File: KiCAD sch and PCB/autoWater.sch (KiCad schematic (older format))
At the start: 14 parts

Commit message: some sch changes
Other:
- note added: "делитель для датчика почвы продумать"
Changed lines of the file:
@@
 Wire Wire Line
 	5050 1450 5050 1400
+Text Notes 7700 3850 0    50   ~ 0
+делитель для датчика почвы продумать
 $EndSCHEMATC

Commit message: some commit
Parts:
- removed Q?: 2N3904, Package_TO_SOT_THT:TO-92_Inline, symbol Transistor_BJT:2N3904
- removed R?: 220, symbol Device:R
- added J2: PROG, Connector_PinHeader_2.54mm:PinHeader_1x05_P2.54mm_Vertical, symbol Connector:Conn_01x05_Male
- added Q2: AO3400, Package_TO_SOT_SMD:SOT-23, symbol Device:Q_NMOS_GSD
- added R3: 1.5k, Resistor_THT:R_Axial_DIN0411_L9.9mm_D3.6mm_P15.24mm_Horizontal, symbol Device:R
- added R5: 10k, Resistor_SMD:R_0805_2012Metric_Pad1.15x1.40mm_HandSolder, symbol Device:R
- added SW1: SW_Push_Dual, Button_Switch_SMD:SW_SPST_Omron_B3FS-100xP, symbol Switch:SW_Push_Dual
- C1: renamed from C?; footprint (none) -> Capacitor_SMD:C_0805_2012Metric_Pad1.15x1.40mm_HandSolder
- D1: renamed from D?; footprint (none) -> LED_SMD:LED_0805_2012Metric_Pad1.15x1.40mm_HandSolder
- J1, J3, J4: renamed from J?; footprint (none) -> Connector_PinHeader_2.54mm:PinHeader_1x02_P2.54mm_Vertical
- Q1: renamed from Q?; footprint (none) -> Package_TO_SOT_SMD:SOT-23
- R1, R4, R6: renamed from R?; footprint (none) -> Resistor_SMD:R_0805_2012Metric_Pad1.15x1.40mm_HandSolder
- R2: renamed from R?; value 100k -> 4.7k; footprint (none) -> Resistor_THT:R_Axial_DIN0411_L9.9mm_D3.6mm_P15.24mm_Horizontal
- R7: renamed from R?; value 130k -> 150k; footprint (none) -> Resistor_SMD:R_0805_2012Metric_Pad1.15x1.40mm_HandSolder
- gave numbers to parts that had none: 1
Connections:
- net +5V: now also J2.4 (Pin_4)
- net GND: now also J2.5 (Pin_5), Q2.2 (S), R3.2, R5.2, SW1.2, SW1.4; no longer R2.2
- net Sensor: no longer U1.3 (PB4)
- net Button: now reaches U1.1 (~RESET~/PB5)
- net Button: now also SW1.1, SW1.3
- net at U1.2 (PB3): now also Q2.1 (G), R5.1
- net at R1.2, U1.5 (PB0): now also J2.2 (Pin_2)
- net at Q1.1 (G), R4.1, U1.6 (PB1): now also J2.3 (Pin_3)
- net at R6.2, R7.1, U1.7 (PB2): now also J2.1 (Pin_1)
- net at J3.2 (Pin_2): now also Q2.3 (D)
- new net: R2.2, R3.1, U1.3 (PB4)
- no-connect marks 1 -> 0
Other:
- note added: "2n3904 + 220 Ohm"
- note added: "делитель нужен, чтобы понизить\nнапряжения для сравнения с\nопорным 1.1В"
- note removed: "делитель для датчика почвы продумать"
- moved on the sheet: J3, R2

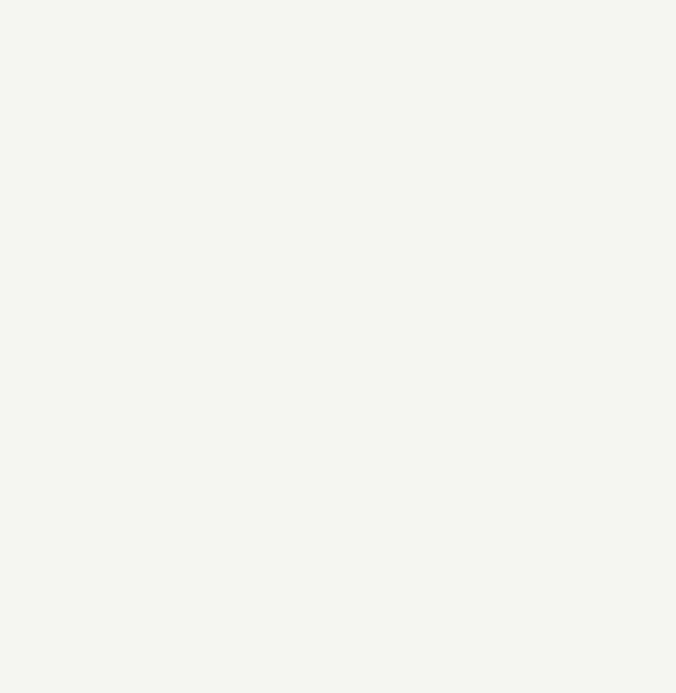
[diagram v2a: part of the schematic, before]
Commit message: added li ion charger on pcb
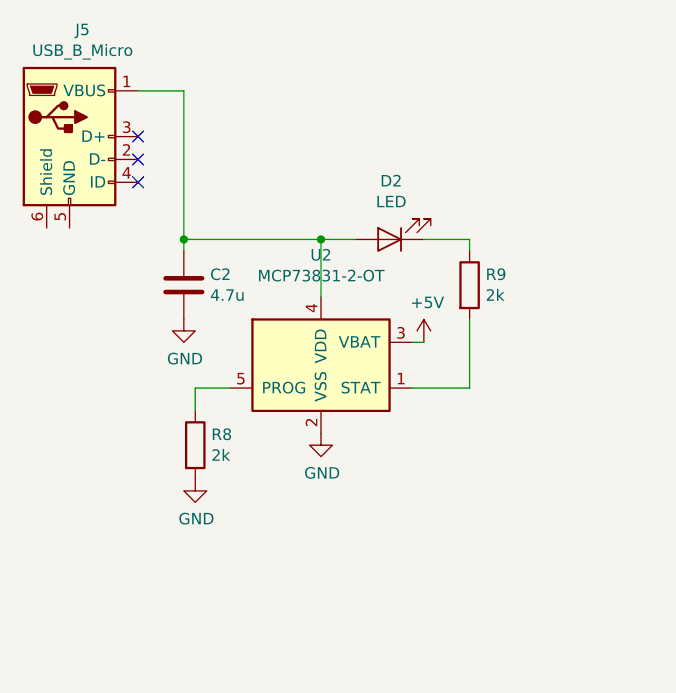
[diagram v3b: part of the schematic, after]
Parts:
- added C2: 4.7u, Capacitor_SMD:C_0805_2012Metric_Pad1.15x1.40mm_HandSolder, symbol Device:C
- added D2: LED, LED_SMD:LED_0805_2012Metric_Pad1.15x1.40mm_HandSolder, symbol Device:LED
- added J5: USB_B_Micro, Connector_USB:USB_Micro-B_Wuerth_629105150521, symbol Connector:USB_B_Micro
- added R8, R9: 2k, Resistor_SMD:R_0805_2012Metric_Pad1.15x1.40mm_HandSolder, symbol Device:R
- added U2: MCP73831-2-OT, Package_TO_SOT_SMD:SOT-23-5, symbol Battery_Management:MCP73831-2-OT
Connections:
- net +5V: now also U2.3 (VBAT)
- net GND: now also C2.2, R8.2, U2.2 (VSS)
- new net: C2.1, D2.2 (A), J5.1 (VBUS), U2.4 (VDD)
- new net: R8.1, U2.5 (PROG)
- new net: D2.1 (K), R9.1
- new net: R9.2, U2.1 (STAT)
- no-connect marks 0 -> 3
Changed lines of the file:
@@
 	8800 5000 8800 5200
 Connection ~ 8800 5200
+$Comp
+L Connector:USB_B_Micro J5
+U 1 1 5ED77C14
+P 1000 1150
+F 0 "J5" H 1057 1617 50  0000 C CNN
+F 1 "USB_B_Micro" H 1057 1526 50  0000 C CNN
+F 2 "Connector_USB:USB_Micro-B_Wuerth_629105150521" H 1150 1100 50  0001 C CNN
+F 3 "~" H 1150 1100 50  0001 C CNN
+	1    1000 1150
+	1    0    0    -1
+$EndComp
+NoConn ~ 1300 1150
+NoConn ~ 1300 1250
+NoConn ~ 1300 1350
+$Comp
+L Device:R R8
+U 1 1 5ED7E586
+P 1550 2500
+F 0 "R8" H 1620 2546 50  0000 L CNN
+F 1 "2k" H 1620 2455 50  0000 L CNN
+F 2 "Resistor_SMD:R_0805_2012Metric_Pad1.15x1.40mm_HandSolder" V 1480 2500 50  0001 C CNN
+F 3 "~" H 1550 2500 50  0001 C CNN
+	1    1550 2500
+	1    0    0    -1
+$EndComp
+$Comp
+L Battery_Management:MCP73831-2-OT U2
+U 1 1 5ED87504
+P 2100 2150
+F 0 "U2" H 2100 2631 50  0000 C CNN
+F 1 "MCP73831-2-OT" H 2100 2540 50  0000 C CNN
+F 2 "Package_TO_SOT_SMD:SOT-23-5" H 2150 1900 50  0001 L CIN
+F 3 "http://ww1.microchip.com/downloads/en/DeviceDoc/20001984g.pdf" H 1950 2100 50  0001 C CNN
+	1    2100 2150
+	1    0    0    -1
+$EndComp
+Wire Wire Line
+	1700 2250 1550 2250
+Wire Wire Line
+	1550 2250 1550 2350
+$Comp
+L power:GND #PWR02
+U 1 1 5ED80F71
+P 1550 2650
+F 0 "#PWR02" H 1550 2400 50  0001 C CNN
+F 1 "GND" H 1555 2477 50  0000 C CNN
+F 2 "" H 1550 2650 50  0001 C CNN
+F 3 "" H 1550 2650 50  0001 C CNN
+	1    1550 2650
+	1    0    0    -1
+$EndComp
+$Comp
+L power:GND #PWR03
+U 1 1 5ED8174D
+P 2100 2450
+F 0 "#PWR03" H 2100 2200 50  0001 C CNN
+F 1 "GND" H 2105 2277 50  0000 C CNN
+F 2 "" H 2100 2450 50  0001 C CNN
+F 3 "" H 2100 2450 50  0001 C CNN
+	1    2100 2450
+	1    0    0    -1
+$EndComp
+$Comp
+L Device:LED D2
+U 1 1 5ED81BE4
+P 2400 1600
+F 0 "D2" H 2393 1345 50  0000 C CNN
+F 1 "LED" H 2393 1436 50  0000 C CNN
+F 2 "LED_SMD:LED_0805_2012Metric_Pad1.15x1.40mm_HandSolder" H 2400 1600 50  0001 C CNN
+F 3 "~" H 2400 1600 50  0001 C CNN
+	1    2400 1600
+	-1   0    0    1
+$EndComp
+$Comp
+L Device:R R9
+U 1 1 5ED82954
+P 2750 1800
+F 0 "R9" H 2820 1846 50  0000 L CNN
+F 1 "2k" H 2820 1755 50  0000 L CNN
+F 2 "Resistor_SMD:R_0805_2012Metric_Pad1.15x1.40mm_HandSolder" V 2680 1800 50  0001 C CNN
+F 3 "~" H 2750 1800 50  0001 C CNN
+	1    2750 1800
+	1    0    0    -1
+$EndComp
+Wire Wire Line
+	2250 1600 2100 1600
+Wire Wire Line
+	2100 1600 2100 1850
+Wire Wire Line
+	2550 1600 2750 1600
+Wire Wire Line
+	2750 1600 2750 1650
+Wire Wire Line
+	2750 1950 2750 2250
+Wire Wire Line
+	2750 2250 2500 2250
+$Comp
+L Device:C C2
+U 1 1 5ED885A2
+P 1500 1800
+F 0 "C2" H 1615 1846 50  0000 L CNN
+F 1 "4.7u" H 1615 1755 50  0000 L CNN
+F 2 "Capacitor_SMD:C_0805_2012Metric_Pad1.15x1.40mm_HandSolder" H 1538 1650 50  0001 C CNN
+F 3 "~" H 1500 1800 50  0001 C CNN
+	1    1500 1800
+	1    0    0    -1
+$EndComp
+Wire Wire Line
+	2100 1600 1500 1600
+Wire Wire Line
+	1500 1600 1500 1650
+Connection ~ 2100 1600
+Wire Wire Line
+	1500 1600 1500 950
+Wire Wire Line
+	1500 950  1300 950
+Connection ~ 1500 1600
+$Comp
+L power:GND #PWR01
+U 1 1 5ED90F67
+P 1500 1950
+F 0 "#PWR01" H 1500 1700 50  0001 C CNN
+F 1 "GND" H 1505 1777 50  0000 C CNN
+F 2 "" H 1500 1950 50  0001 C CNN
+F 3 "" H 1500 1950 50  0001 C CNN
+	1    1500 1950
+	1    0    0    -1
+$EndComp
+$Comp
+L power:+5V #PWR04
+U 1 1 5ED912FB
+P 2550 2050
+F 0 "#PWR04" H 2550 1900 50  0001 C CNN
+F 1 "+5V" H 2565 2223 50  0000 C CNN
+F 2 "" H 2550 2050 50  0001 C CNN
+F 3 "" H 2550 2050 50  0001 C CNN
+	1    2550 2050
+	1    0    0    -1
+$EndComp
+Wire Wire Line
+	2500 2050 2550 2050
 $EndSCHEMATC

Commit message: same
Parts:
- R9: value 2k -> 470
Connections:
- net GND: now also J5.5 (GND), J5.6 (Shield)
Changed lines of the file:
@@
 P 2750 1800
 F 0 "R9" H 2820 1846 50  0000 L CNN
-F 1 "2k" H 2820 1755 50  0000 L CNN
+F 1 "470" H 2820 1755 50  0000 L CNN
 F 2 "Resistor_SMD:R_0805_2012Metric_Pad1.15x1.40mm_HandSolder" V 2680 1800 50  0001 C CNN
 F 3 "~" H 2750 1800 50  0001 C CNN
@@
 Wire Wire Line
 	2500 2050 2550 2050
+$Comp
+L power:GND #PWR0118
+U 1 1 5EDA0745
+P 1000 1550
+F 0 "#PWR0118" H 1000 1300 50  0001 C CNN
+F 1 "GND" H 1005 1377 50  0000 C CNN
+F 2 "" H 1000 1550 50  0001 C CNN
+F 3 "" H 1000 1550 50  0001 C CNN
+	1    1000 1550
+	1    0    0    -1
+$EndComp
+Wire Wire Line
+	900  1550 1000 1550
+Connection ~ 1000 1550
 $EndSCHEMATC

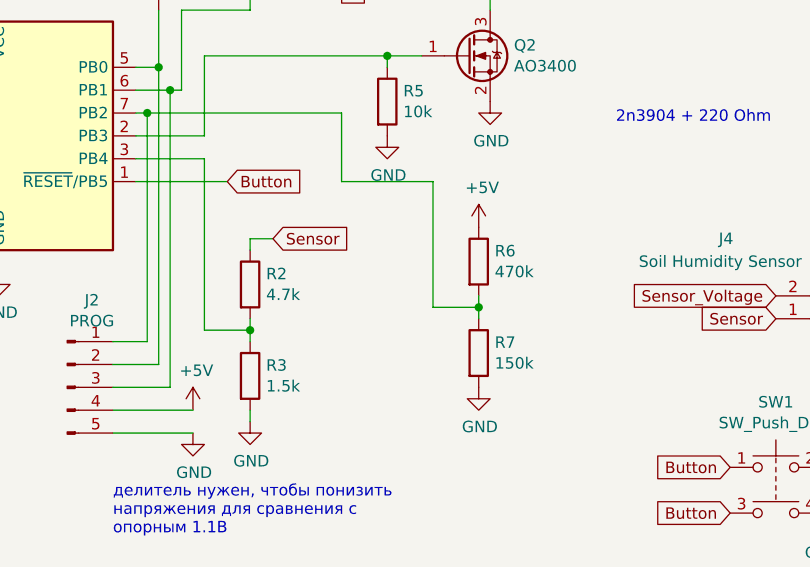
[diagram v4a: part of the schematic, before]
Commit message: resistor value change
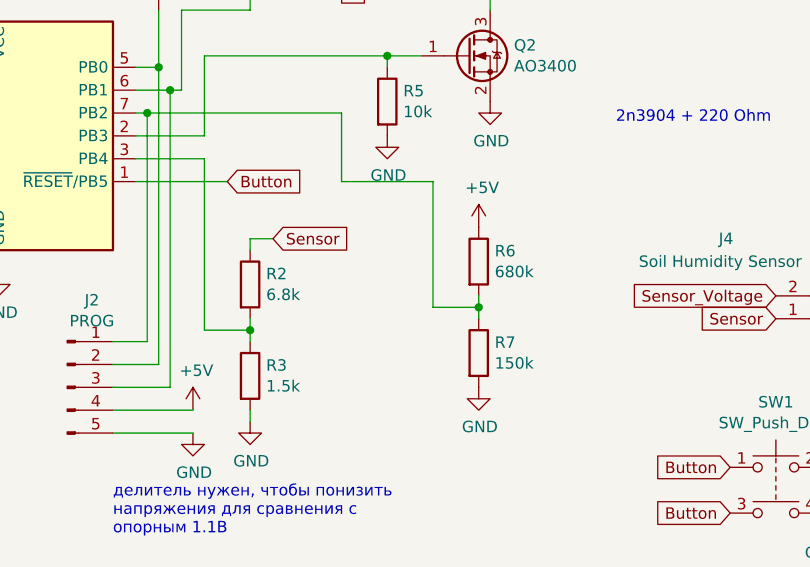
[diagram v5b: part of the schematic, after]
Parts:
- R2: value 4.7k -> 6.8k
- R6: value 470k -> 680k
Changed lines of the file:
@@
 P 7300 4100
 F 0 "R6" H 7370 4146 50  0000 L CNN
-F 1 "470k" H 7370 4055 50  0000 L CNN
+F 1 "680k" H 7370 4055 50  0000 L CNN
 F 2 "Resistor_SMD:R_0805_2012Metric_Pad1.15x1.40mm_HandSolder" V 7230 4100 50  0001 C CNN
 F 3 "~" H 7300 4100 50  0001 C CNN
@@
 P 6300 4200
 F 0 "R2" H 6370 4246 50  0000 L CNN
-F 1 "4.7k" H 6370 4155 50  0000 L CNN
+F 1 "6.8k" H 6370 4155 50  0000 L CNN
 F 2 "Resistor_THT:R_Axial_DIN0411_L9.9mm_D3.6mm_P15.24mm_Horizontal" V 6230 4200 50  0001 C CNN
 F 3 "~" H 6300 4200 50  0001 C CNN

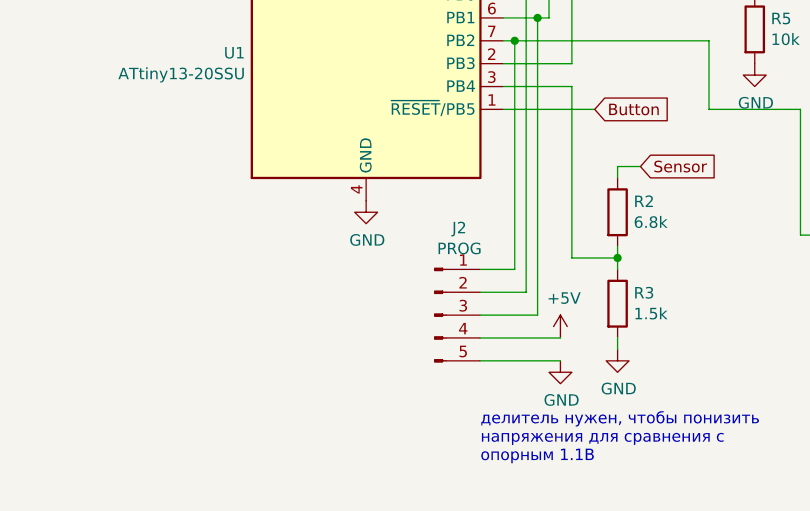
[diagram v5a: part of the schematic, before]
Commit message: text on sch
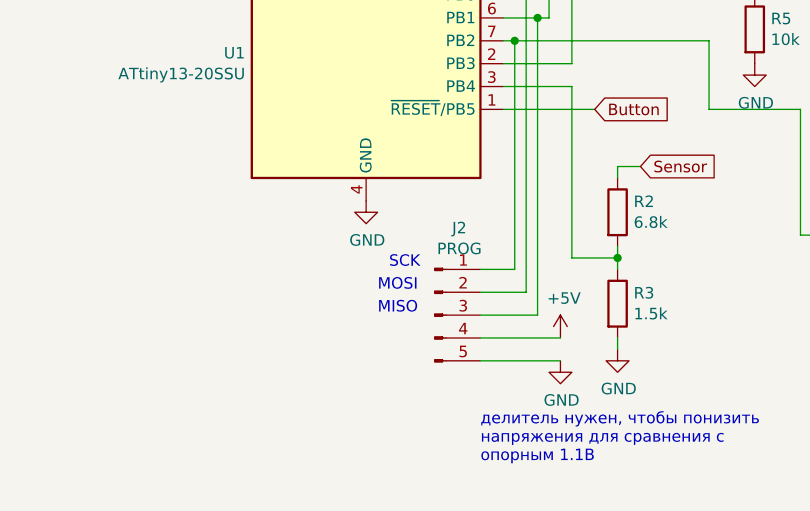
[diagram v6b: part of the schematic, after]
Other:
- note added: "MISO"
- note added: "MOSI"
- note added: "SCK\n"
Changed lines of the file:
@@
 	900  1550 1000 1550
 Connection ~ 1000 1550
+Text Notes 5300 4450 0    50   ~ 0
+SCK\n
+Text Notes 5250 4550 0    50   ~ 0
+MOSI
+Text Notes 5250 4650 0    50   ~ 0
+MISO
 $EndSCHEMATC

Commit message: add readme & small code changes
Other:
- note removed: "Необходимо проверить\nсоответствие выводов"
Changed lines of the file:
@@
 Wire Wire Line
 	4800 2450 5200 2450
-Text Notes 6950 2000 0    50   ~ 0
-Необходимо проверить\nсоответствие выводов
 $Comp
 L Connector:Conn_01x02_Male J1
